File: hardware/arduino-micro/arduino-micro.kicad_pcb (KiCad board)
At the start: 2 copper layers, 76.2 x 43.2 mm, 9 parts, among them J1 PJ-028-SMT-TR, M1 Fan_4pin, SW1 Rotary_Encoder, U1 TM1637, U2 CA56-12CGKWA

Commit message: fixes for cnc'd pcb
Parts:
- added C1: 100uF, Capacitor_THT:CP_Radial_Tantal_D4.5mm_P2.50mm, F.Cu at (223.5, 128.3)
- added C2: 0.1uF, Capacitor_SMD:C_0805_2012Metric, F.Cu at (219.7, 124.1)
- added C3: 100pF, Capacitor_SMD:C_0805_2012Metric, F.Cu at (210.8, 116.8)
- added C4: 100pF, Capacitor_SMD:C_0805_2012Metric, F.Cu at (221.0, 116.8)
- added R4: 10k, Resistor_SMD:R_0805_2012Metric, F.Cu at (213.4, 116.8)
- added R5: 10k, Resistor_SMD:R_0805_2012Metric, F.Cu at (218.4, 116.8)
- M1: moved to B.Cu
- R1, R2, R3: footprint LED_SMD:LED_0805_2012Metric -> Resistor_SMD:R_0805_2012Metric
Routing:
- net GND: track 80.8 -> 137.9 mm, vias 1 -> 3
- net /5V: track 77.1 -> 116.4 mm, vias 0 -> 3
- net /7S_IO: track 17.5 -> 34.1 mm, vias 0 -> 1
- net /7S_CLK: track 34.8 -> 48.6 mm, vias 0 -> 1
- net Net-(M1-Pad4): track 37.5 -> 43.2 mm, vias 0 -> 1
- net Net-(M1-Pad3): track 50.1 -> 45.9 mm, vias 0 -> 1
- net Net-(U1-Pad3): track 19.3 -> 21.7 mm, vias 1 -> 2
- net Net-(R1-Pad2): track 67.7 -> 68.0 mm, vias 0 -> 1
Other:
- board size 76.2 x 43.2 mm -> 78.7 x 44.5 mm

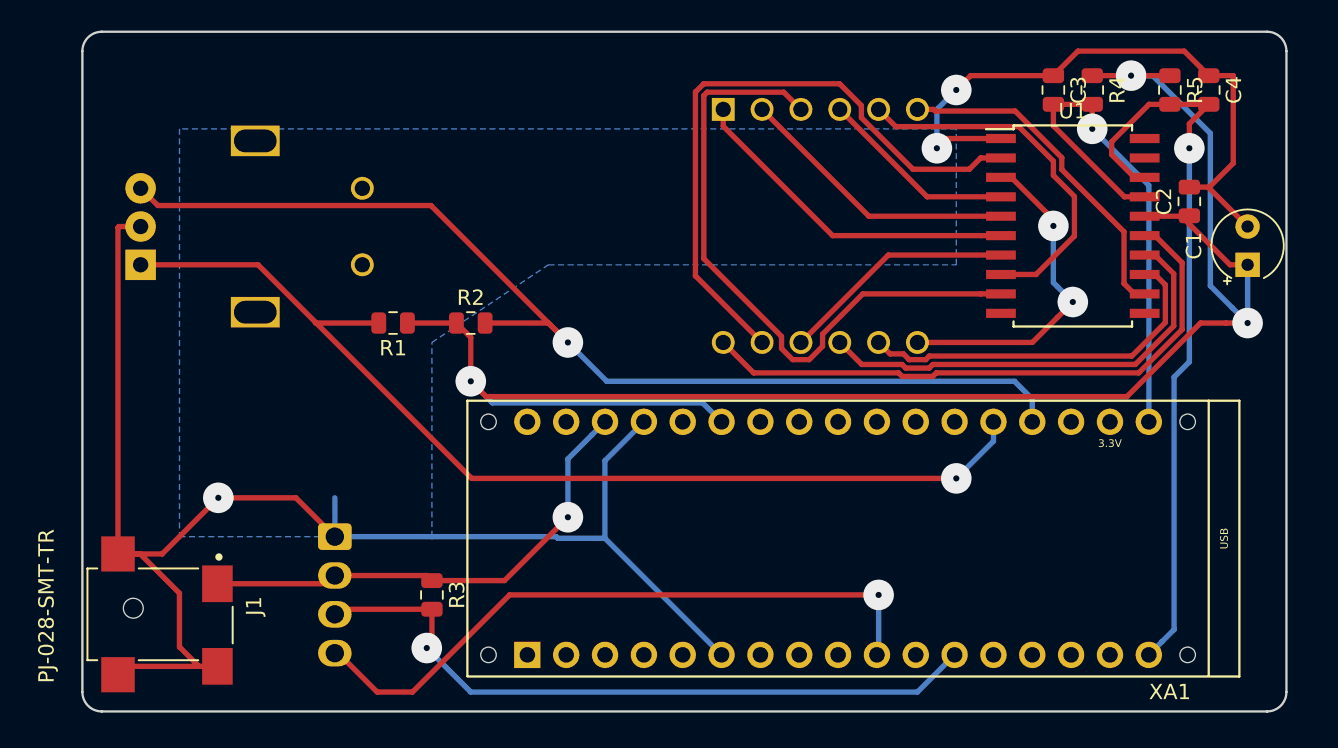
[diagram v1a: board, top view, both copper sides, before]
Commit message: fix too close edge
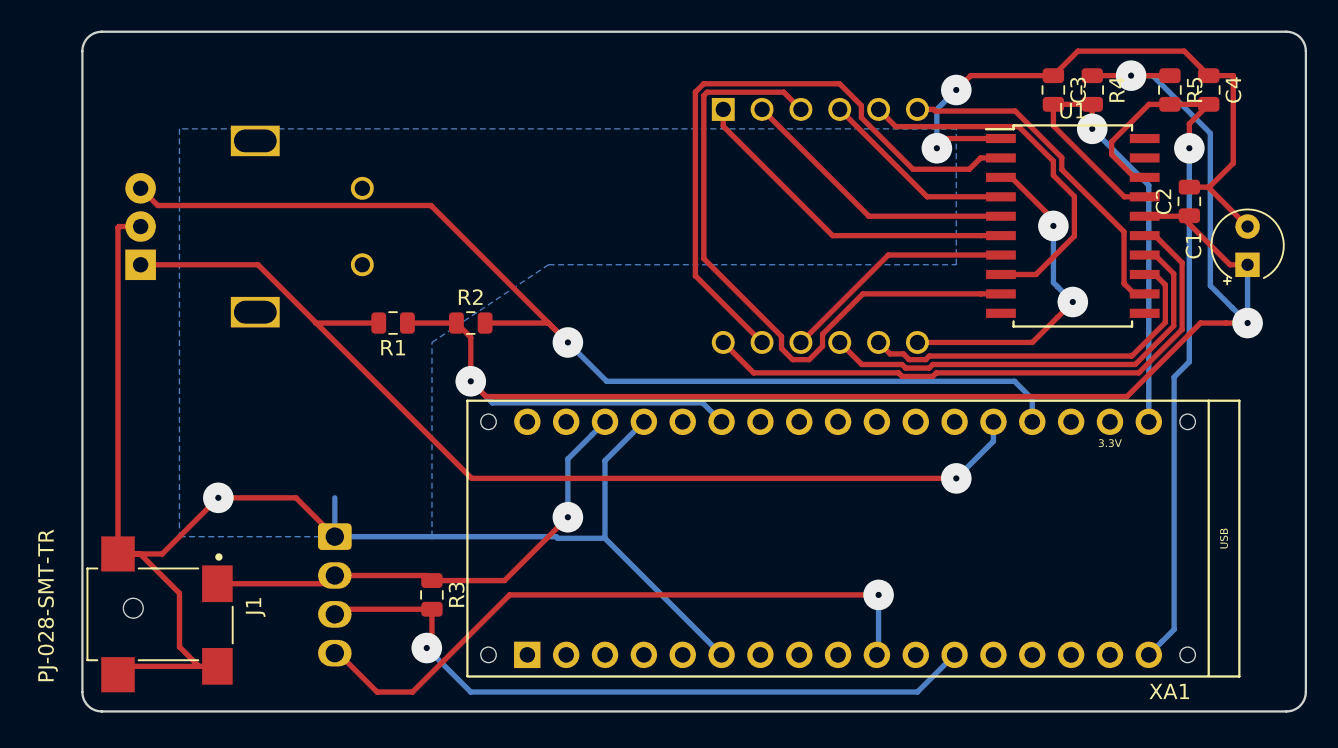
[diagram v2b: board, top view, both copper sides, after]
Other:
- board size 78.7 x 44.5 mm -> 80 x 44.5 mm
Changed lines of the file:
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@@
       (outputformat 1)
       (mirror false)
-      (drillshape 1)
+      (drillshape 0)
       (scaleselection 1)
-      (outputdirectory ""))
+      (outputdirectory "gerbers/"))
   )
   (net 0 "")
@@
     )
   )
-  (gr_line (start 224.79 113.03) (end 148.59 113.03) (layer Edge.Cuts) (width 0.15))
-  (gr_line (start 226.06 114.3) (end 226.06 156.21) (layer Edge.Cuts) (width 0.15))
-  (gr_arc (start 224.79 114.3) (end 226.06 114.3) (angle -90) (layer Edge.Cuts) (width 0.15))
-  (gr_line (start 148.59 157.48) (end 224.79 157.48) (layer Edge.Cuts) (width 0.15))
+  (gr_line (start 226.06 113.03) (end 148.59 113.03) (layer Edge.Cuts) (width 0.15))
+  (gr_line (start 227.33 114.3) (end 227.33 156.21) (layer Edge.Cuts) (width 0.15))
+  (gr_arc (start 226.06 114.3) (end 227.33 114.3) (angle -90) (layer Edge.Cuts) (width 0.15))
+  (gr_line (start 148.59 157.48) (end 226.06 157.48) (layer Edge.Cuts) (width 0.15))
   (gr_line (start 147.32 114.3) (end 147.32 156.21) (layer Edge.Cuts) (width 0.15))
   (gr_arc (start 148.59 114.3) (end 148.59 113.03) (angle -90) (layer Edge.Cuts) (width 0.15))
   (gr_arc (start 148.59 156.21) (end 147.32 156.21) (angle -90) (layer Edge.Cuts) (width 0.15))
-  (gr_arc (start 224.79 156.21) (end 224.79 157.48) (angle -90) (layer Edge.Cuts) (width 0.15))
+  (gr_arc (start 226.06 156.21) (end 226.06 157.48) (angle -90) (layer Edge.Cuts) (width 0.15))
   (segment (start 150.2 154.53) (end 149.65 155.08) (width 0.35) (layer F.Cu) (net 1))
   (segment (start 203.835 120.015) (end 203.2 120.65) (width 0.35) (layer F.Cu) (net 1))
